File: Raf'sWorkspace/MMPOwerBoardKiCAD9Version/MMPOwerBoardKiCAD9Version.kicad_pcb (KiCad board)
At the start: 2 copper layers, 79 x 60 mm, 103 parts, among them J1 TYPE-C-31-M-04, J2 Conn_02x16_Odd_Even, J3 Conn_01x02, Q1 SS8050, SW1 SS-12D11-G050, U1 HUSB237, U10 TPS22917DBVR, U11 AMS1117-5.0, U2 TP4056-42-ESOP8, U3 DRV8833PWPR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

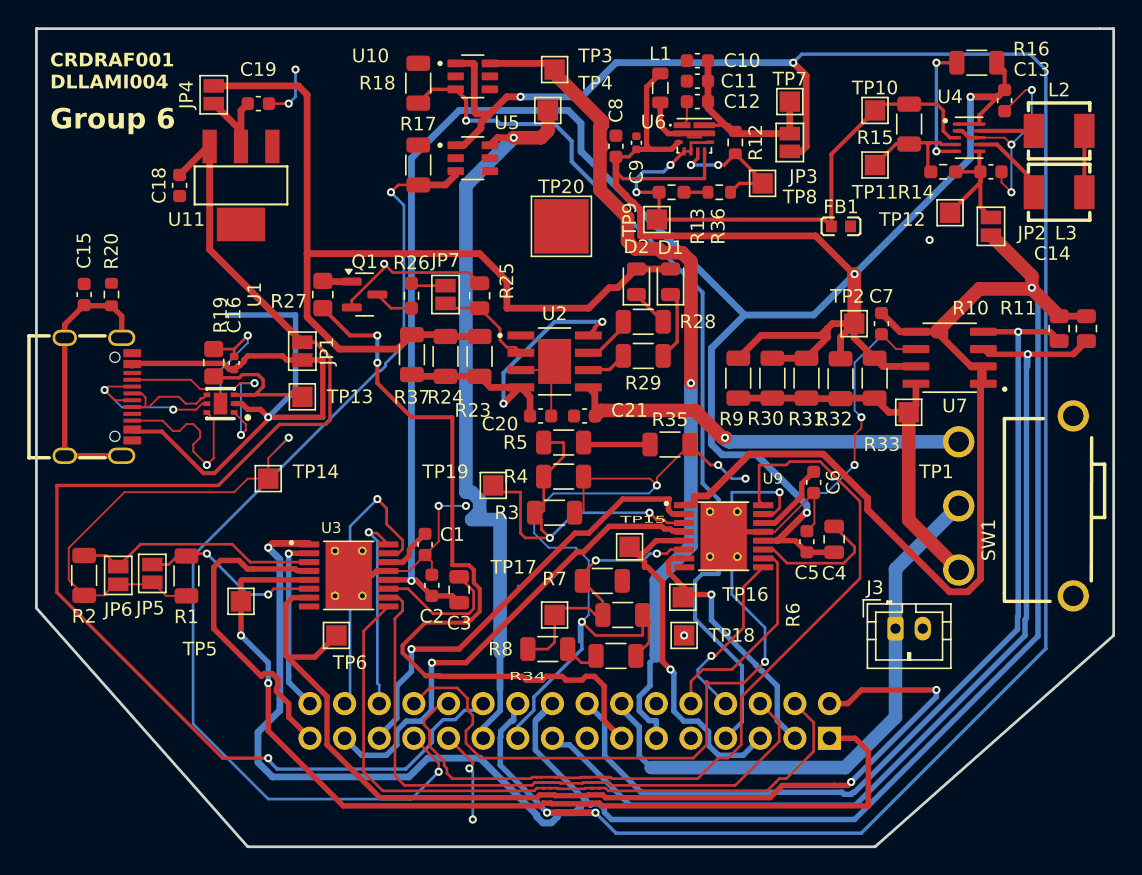
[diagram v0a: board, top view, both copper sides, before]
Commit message: Fixed PCB board, DRC has 0 errors now apparently
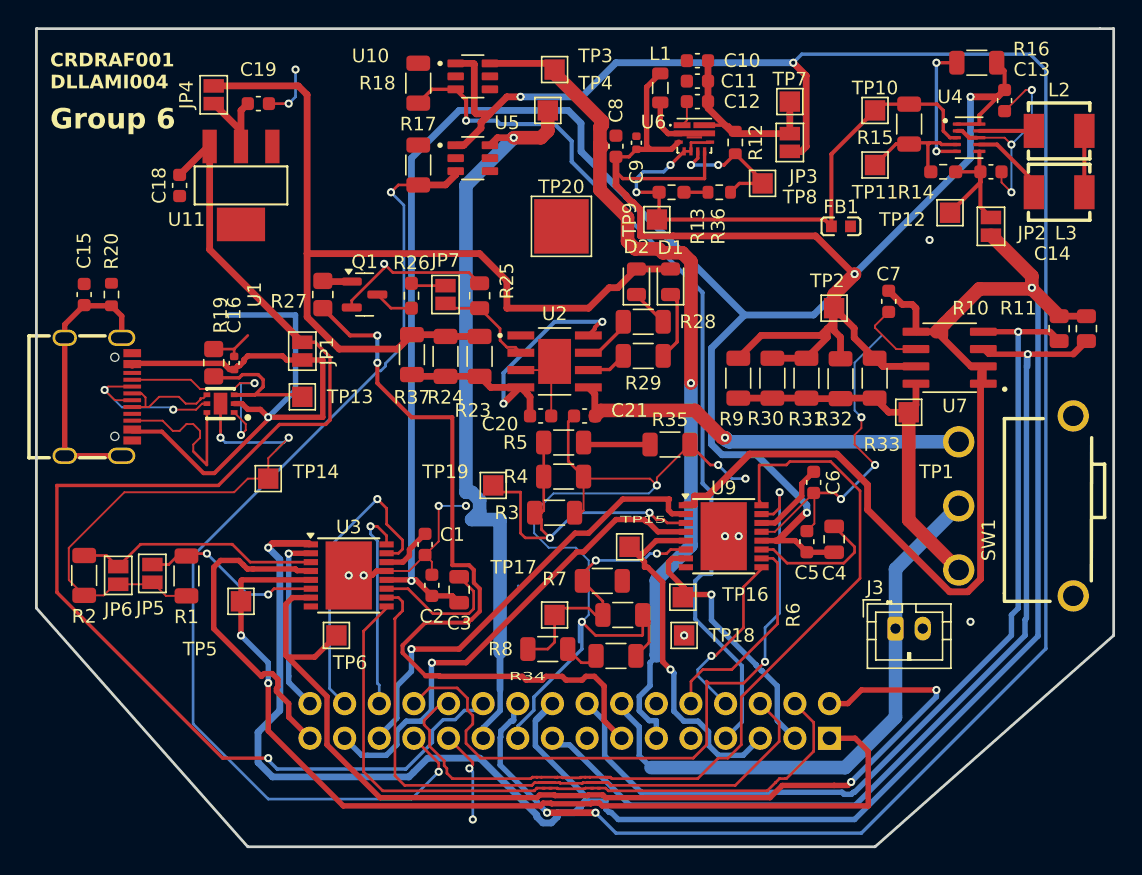
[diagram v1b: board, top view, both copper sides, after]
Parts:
- U3, U9: footprint DRV8833PWPR:IC_DRV8833PWPR -> Package_SO:HTSSOP-16-1EP_4.4x5mm_P0.65mm_EP3.4x5mm
- moved TP2 1.86 mm to (223.0, 69.5)
- moved C7 1.72 mm to (227.0, 69.0)
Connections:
- J1 pad S3: (no net) -> Net-(C15-Pad1)
- J1 pad S4: (no net) -> Net-(C15-Pad1)
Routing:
- net GND: track 195.5 -> 205.9 mm, vias 20 -> 26
- net /MOTOR3_CTRL2: track 57.0 -> 52.6 mm
- net Net-(U9-AISEN): track 28.5 -> 26.5 mm
- net /3V3: track 195.9 -> 197.8 mm
- net /LoadCircuit: track 207.0 -> 208.7 mm
- net /MOTOR1_CTRL2: track 21.6 -> 22.5 mm
- net /MOTOR1_CTRL1: track 14.5 -> 15.4 mm
- net /EXT_LOAD2_CTRL: track 65.7 -> 65.0 mm
- net Net-(J1-CC2): track 13.2 -> 12.7 mm, vias 1 -> 0
- added copper zone on B.Cu, net GND
- added copper zone on F.Cu, net GND

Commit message: Added the JLC PCB submission pcis and stuff [named incorrectedly
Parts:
- J1: value TYPE-C-31-M-04 -> TYPE-C-31-M-12
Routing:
- net GND: track 205.9 -> 203.2 mm
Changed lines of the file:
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@@
 			)
 		)
-		(property "Value" "TYPE-C-31-M-04"
+		(property "Value" "TYPE-C-31-M-12"
 			(at 0 5.921 270)
 			(layer "F.Fab")
@@
 			)
 		)
-		(property "JLC_3DModel_Q" "d4850b6bcfb24c8f8ccb21298ff9a0df"
-			(at 0 0 270)
-			(layer "Cmts.User")
-			(hide yes)
-			(effects
-				(font
-					(size 1.27 1.27)
-					(thickness 0.15)
-				)
-			)
-		)
-		(property "JLC_3D_Size" "8.94 7.9"
-			(at 0 0 270)
-			(layer "Cmts.User")
-			(hide yes)
-			(effects
-				(font
-					(size 1.27 1.27)
-					(thickness 0.15)
-				)
-			)
-		)
 		(property "MF" "HRO Electronics Co., Ltd."
 			(at 0 0 270)
@@
 			)
 		)
-		(property "LCSC" "C129018"
+		(property "LCSC" "C165948"
 			(at 0 0 270)
 			(unlocked yes)
@@
 			(remove_unused_layers no)
 			(net 10 "Net-(C15-Pad1)")
+			(pinfunction "SHIELD")
+			(pintype "passive")
 		)
 		(pad "S2" thru_hole oval
@@
 			(remove_unused_layers no)
 			(net 10 "Net-(C15-Pad1)")
+			(pinfunction "SHIELD")
+			(pintype "passive")
 		)
 		(pad "S3" thru_hole oval
@@
 			(remove_unused_layers no)
 			(net 10 "Net-(C15-Pad1)")
+			(pinfunction "SHIELD")
+			(pintype "passive")
 		)
 		(pad "S4" thru_hole oval
@@
 			(remove_unused_layers no)
 			(net 10 "Net-(C15-Pad1)")
+			(pinfunction "SHIELD")
+			(pintype "passive")
 		)
 		(embedded_fonts no)
@@
 		(sheetname "/")
 		(sheetfile "MMPOwerBoardKiCAD9Version.kicad_sch")
-		(attr exclude_from_pos_files exclude_from_bom)
+		(attr exclude_from_pos_files)
 		(fp_line
 			(start -2.2 -2.2)
@@
 	)
 	(segment
-		(start 204.4625 84.5)
-		(end 204.625775 84.336725)
-		(width 0.14)
-		(layer "F.Cu")
-		(net 1)
-	)
-	(segment
 		(start 170.5 89.75)
 		(end 172.85 89.75)
@@
 		(width 0.14)
 		(layer "F.Cu")
-		(net 1)
-	)
-	(segment
-		(start 204.625775 84.336725)
-		(end 204.625775 81.85191)
-		(width 0.14)
-		(layer "F.Cu")

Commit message: Final files for resubmit attached in Final Workspace-> Final
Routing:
- net GND: vias 26 -> 22
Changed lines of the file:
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@@
 	)
 	(via
-		(at 216 86.225)
-		(size 0.6)
-		(drill 0.3)
-		(layers "F.Cu" "B.Cu")
-		(net 1)
-	)
-	(via
 		(at 183 79)
 		(size 0.6)
@@
 	)
 	(via
-		(at 187.4 89.1)
-		(size 0.6)
-		(drill 0.3)
-		(layers "F.Cu" "B.Cu")
-		(net 1)
-	)
-	(via
 		(at 214.5 81)
 		(size 0.6)
@@
 		(net 1)
 	)
-	(via
-		(at 215 86.225)
-		(size 0.6)
-		(drill 0.3)
-		(layers "F.Cu" "B.Cu")
-		(net 1)
-	)
-	(via
-		(at 188.5 89.1)
-		(size 0.6)
-		(drill 0.3)
-		(layers "F.Cu" "B.Cu")
-		(net 1)
-	)
 	(segment
 		(start 236 57.5)
@@
 	)
 	(segment
-		(start 214 95)
-		(end 214.28616 95)
+		(start 218 91.28616)
+		(end 218 88.7)
 		(width 0.2)
 		(layer "F.Cu")
@@
 	)
 	(segment
-		(start 216.349 89.951)
-		(end 217.8 88.5)
+		(start 214 95)
+		(end 214.28616 95)
 		(width 0.2)
 		(layer "F.Cu")
@@
 	)
 	(segment
-		(start 216.349 92.93716)
-		(end 216.349 89.951)
+		(start 218 88.7)
+		(end 217.8 88.5)
 		(width 0.2)
 		(layer "F.Cu")
@@
 	(segment
 		(start 214.28616 95)
-		(end 216.349 92.93716)
+		(end 218 91.28616)
 		(width 0.2)
 		(layer "F.Cu")
